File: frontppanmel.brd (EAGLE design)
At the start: 128.5 x 91.3 mm, 4 parts

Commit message: v0.1.0.1
final V0101
INcluded board., schematic en frontpanel pcb
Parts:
- moved U$1 40.6 mm to (3.00, 83.6)
- moved U$3 40.6 mm to (125.5, 83.6)
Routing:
- net DECO: track 0.00 -> 1161.2 mm
- net N$26: track 0.00 -> 37.0 mm
- net N$51: track 0.00 -> 31.4 mm
- net N$52: track 0.00 -> 29.4 mm
- net N$53: track 0.00 -> 26.4 mm
- net N$54: track 0.00 -> 23.4 mm
- net N$13: track 0.00 -> 21.0 mm
- net N$55: track 0.00 -> 19.4 mm
- net N$25: track 0.00 -> 19.0 mm
- net N$17: track 0.00 -> 19.0 mm
- net N$24: track 0.00 -> 17.0 mm
- net N$16: track 0.00 -> 17.0 mm
- net N$74: track 0.00 -> 16.0 mm
- net N$73: track 0.00 -> 16.0 mm
- net N$72: track 0.00 -> 16.0 mm
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- added copper zone on layer 1, net N$79
- added copper zone on layer 1, net N$84
- added copper zone on layer 1, net N$85
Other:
- board text added: "BIAS"
- board text added: "CUT"
- board text added: "FBG CV"
- board text added: "FEED"
- board text added: "FM CV"
- board text added: "Feedbackgain"
- board text added: "Input"
- board text added: "LEDCompressor"
- board text added: "Leakback"
- board text added: "Muffle CV"
- board text added: "Mufflepass"
- board text added: "Resonator"
- board text added: "STAGE 1"
- board text added: "STAGE 2"
- board text added: "STAGE 3"
- board text added: "Starve"
- board text removed: "Music Thing Modular musicthing.co.uk Turing Machine Panel January 2016 CC-BY-SA"

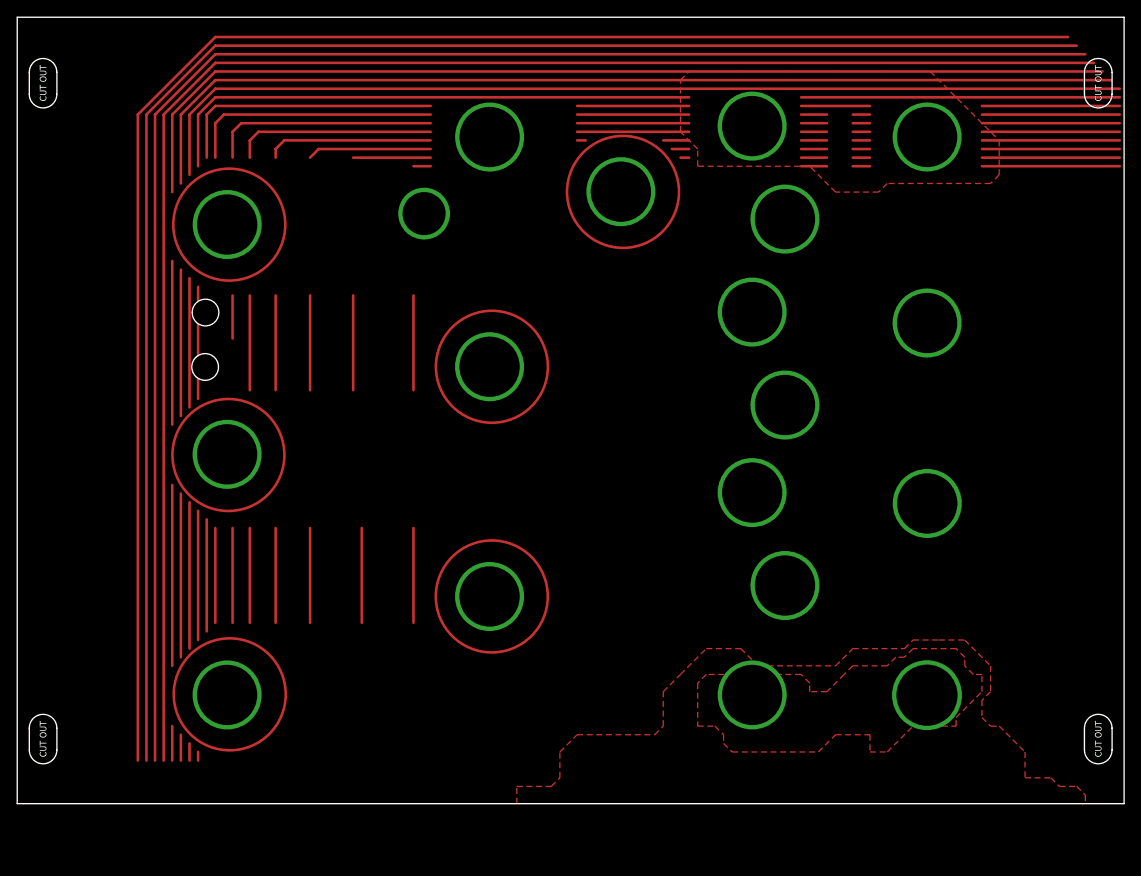
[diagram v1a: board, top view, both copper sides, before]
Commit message: Frontpsanel added
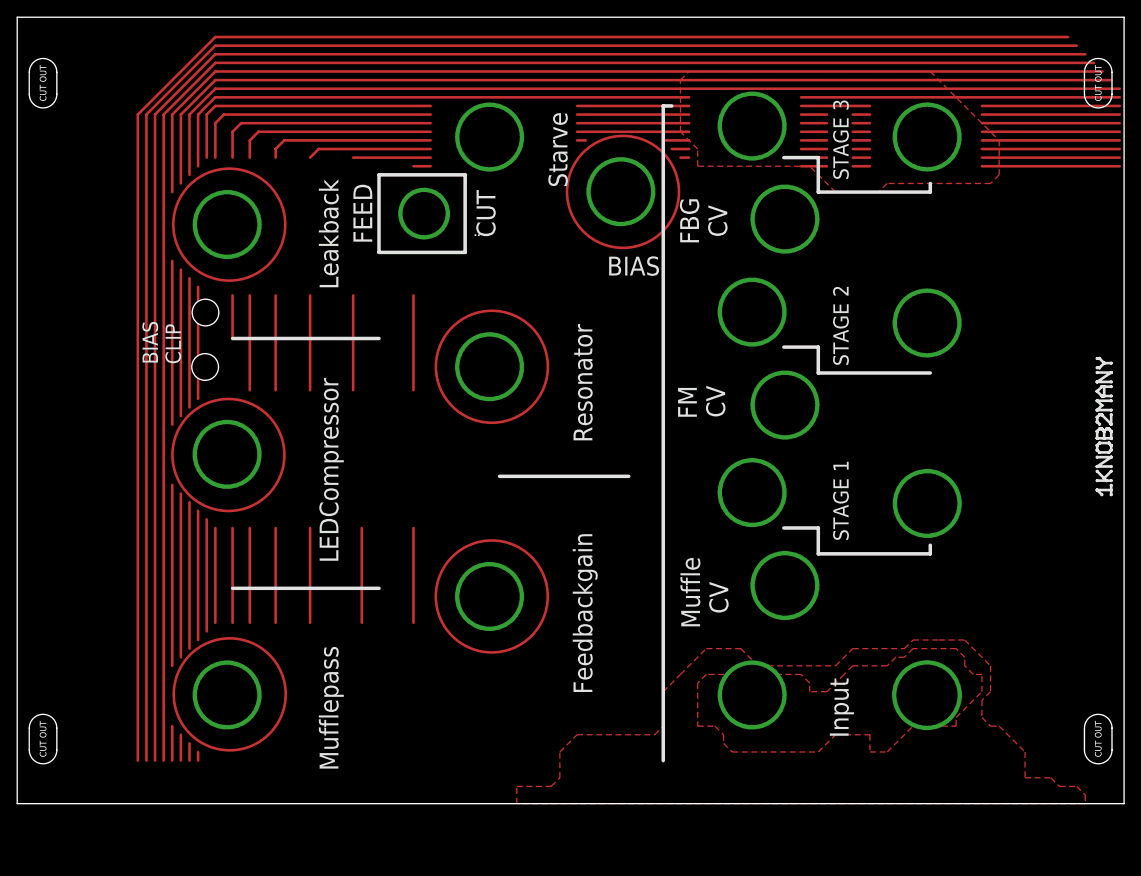
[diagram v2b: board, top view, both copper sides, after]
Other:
- board text added: "BIAS CLIP"
